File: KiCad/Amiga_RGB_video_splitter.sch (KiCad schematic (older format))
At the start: 14 parts, among them J1 DB23_Female-Connector, J2 DB15_Female_HighDensity_Mount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, J3 KMDGX-9S-BS-1, J4 PJ-320A, J5 Conn_01x03, U1 THS7374IPWR, U2 74HCT2G17

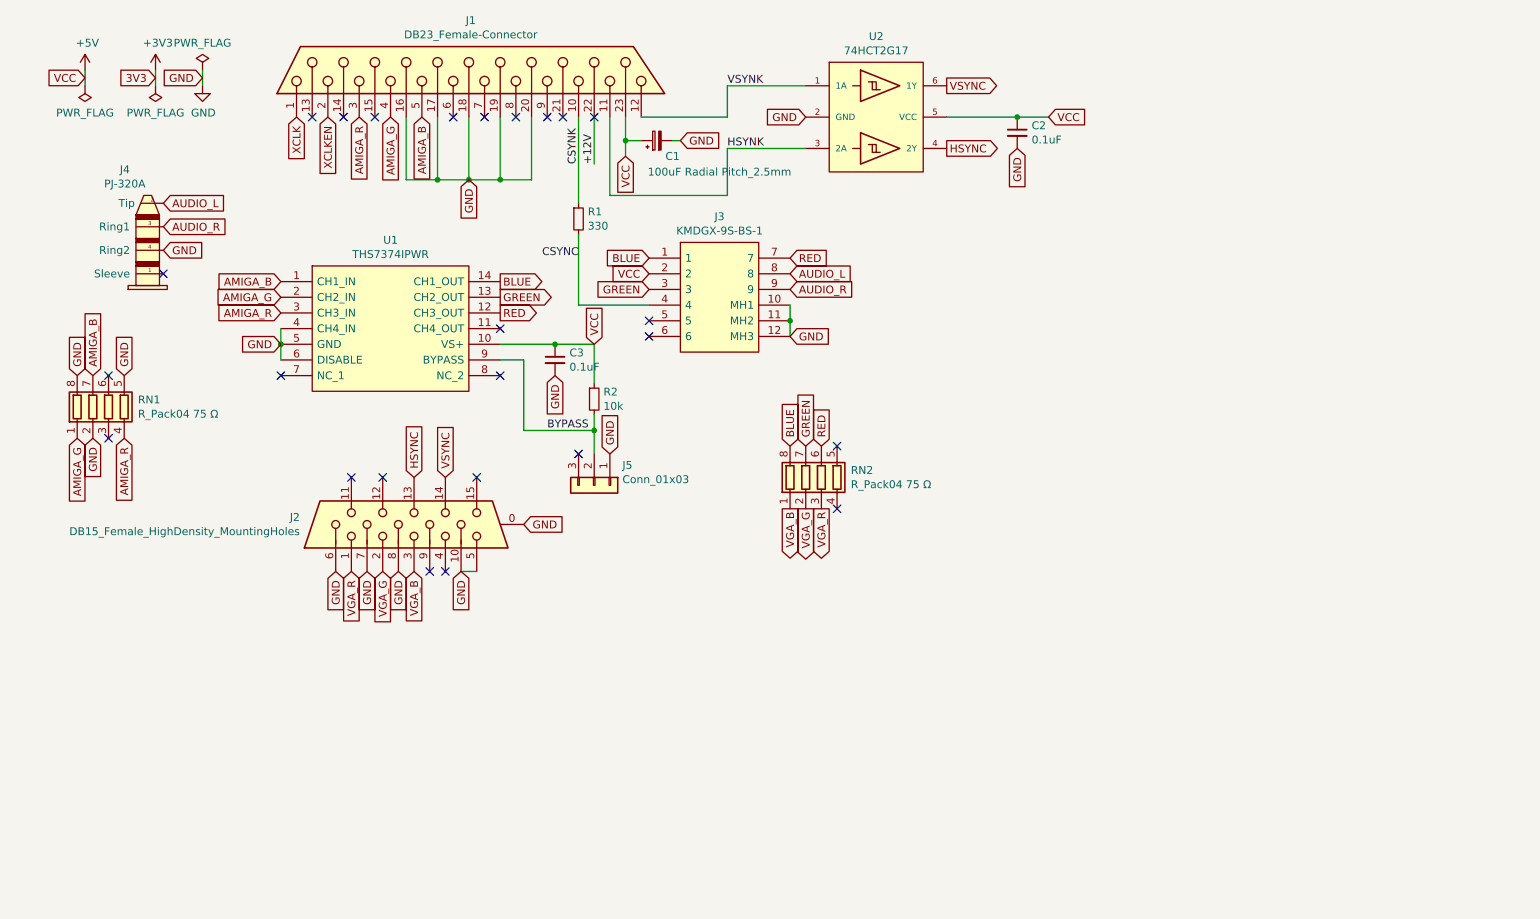
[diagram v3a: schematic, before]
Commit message: Add U3 (74HCT2G14) and R3,R4,C4,C5 to the design
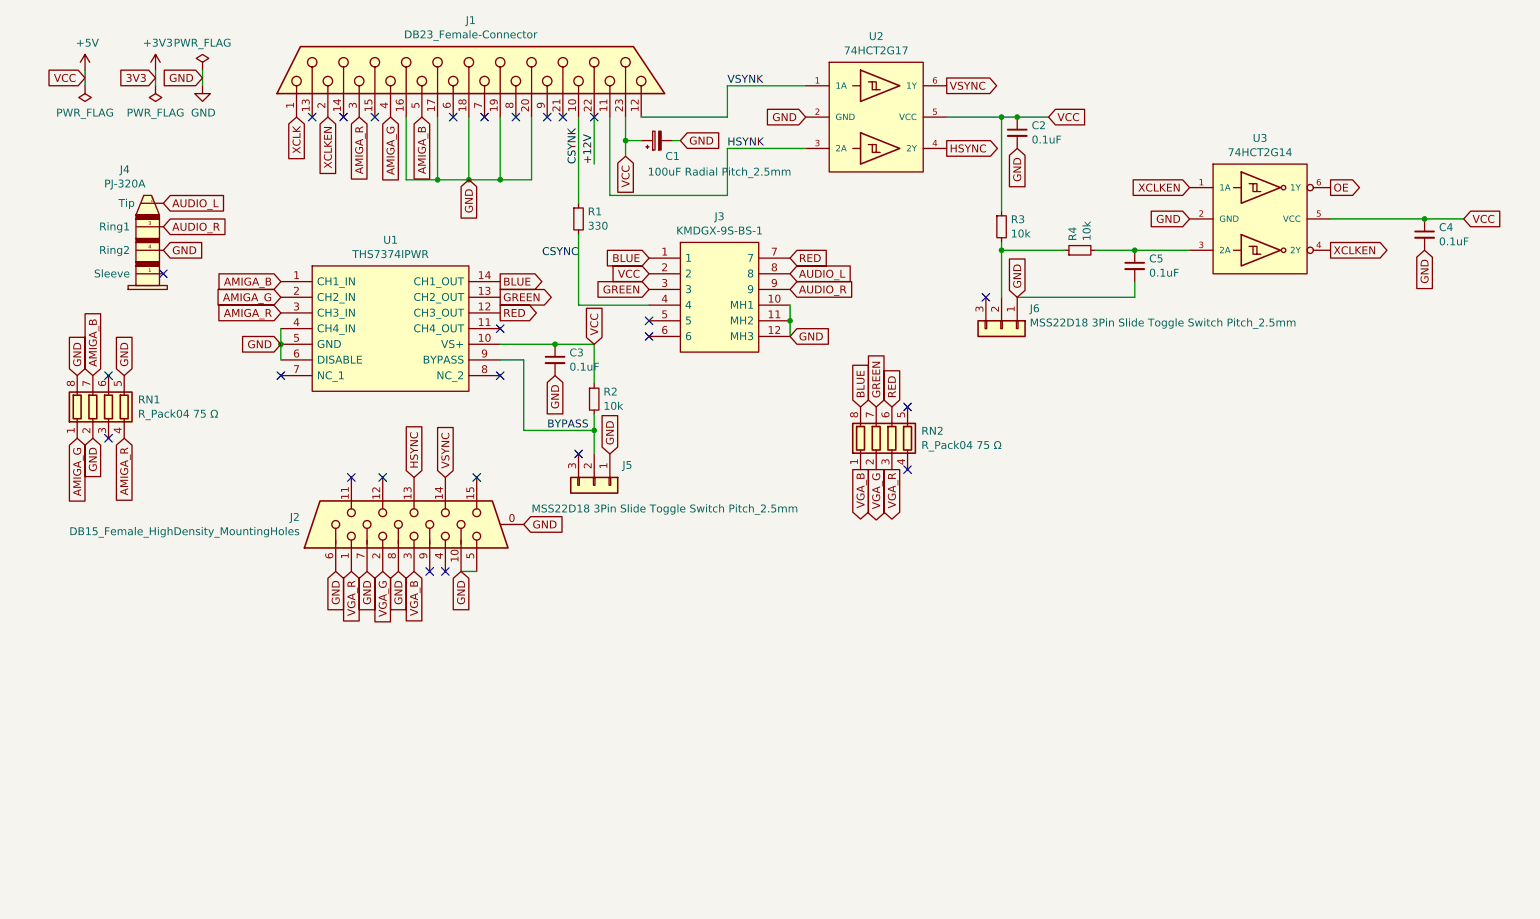
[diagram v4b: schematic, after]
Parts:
- added C4, C5: 0.1uF, Capacitor_SMD:C_0805_2012Metric_Pad1.18x1.45mm_HandSolder, symbol Device:C_Small
- added J6: MSS22D18 3Pin Slide Toggle Switch Pitch_2.5mm, Amiga_RGB_video_splitter:PinHeader_1x03_P2.5mm_Vertical, symbol Connector_Generic:Conn_01x03
- added R3, R4: 10k, Resistor_SMD:R_1206_3216Metric_Pad1.30x1.75mm_HandSolder, symbol Device:R_Small
- added U3: 74HCT2G14, Package_SO:TSOP-6_1.65x3.05mm_P0.95mm, symbol Amiga_RGB_video_splitter:74HCT2G14
- J5: value Conn_01x03 -> MSS22D18 3Pin Slide Toggle Switch Pitch_2.5mm
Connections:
- net +5V: now also C4.1, R3.1, U3.5 (VCC)
- net GND: now also C4.2, C5.2, J6.1 (Pin_1), U3.2 (GND)
- net XCLKEN: now also U3.1 (1A), U3.4 (2Y)
- new net: J6.2 (Pin_2), R3.2, R4.1
- new net: C5.1, R4.2, U3.3 (2A)
- new net OE: U3.6 (1Y)
- no-connect marks 25 -> 26
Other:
- moved on the sheet: RN2
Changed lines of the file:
@@
 L Device:R_Pack04 RN2
 U 1 1 68354B66
-P 5850 5000
-F 0 "RN2" H 6038 5046 50  0000 L CNN
-F 1 "R_Pack04 75 Ω" H 6038 4955 50  0000 L CNN
-F 2 "Amiga_RGB_video_splitter:RESCAF80P320X160X60-8N" V 6125 5000 50  0001 C CNN
-F 3 "~" H 5850 5000 50  0001 C CNN
-	1    5850 5000
-	1    0    0    -1
-$EndComp
-Text GLabel 5650 4800 1    50   Input ~ 0
+P 6300 4750
+F 0 "RN2" H 6488 4796 50  0000 L CNN
+F 1 "R_Pack04 75 Ω" H 6488 4705 50  0000 L CNN
+F 2 "Amiga_RGB_video_splitter:RESCAF80P320X160X60-8N" V 6575 4750 50  0001 C CNN
+F 3 "~" H 6300 4750 50  0001 C CNN
+	1    6300 4750
+	1    0    0    -1
+$EndComp
+Text GLabel 6100 4550 1    50   Input ~ 0
 BLUE
-Text GLabel 5750 4800 1    50   Input ~ 0
+Text GLabel 6200 4550 1    50   Input ~ 0
 GREEN
-Text GLabel 5850 4800 1    50   Input ~ 0
+Text GLabel 6300 4550 1    50   Input ~ 0
 RED
-Text GLabel 5650 5200 3    50   Output ~ 0
+Text GLabel 6100 4950 3    50   Output ~ 0
 VGA_B
-Text GLabel 5750 5200 3    50   Output ~ 0
+Text GLabel 6200 4950 3    50   Output ~ 0
 VGA_G
-Text GLabel 5850 5200 3    50   Output ~ 0
+Text GLabel 6300 4950 3    50   Output ~ 0
 VGA_R
 $Comp
@@
 VSYNK
 Wire Wire Line
-	6650 2700 7100 2700
+	6650 2700 7000 2700
 Wire Wire Line
 	5250 2900 5750 2900
 Text Label 5250 2900 0    50   ~ 0
 HSYNK
-NoConn ~ 5950 4800
-NoConn ~ 5950 5200
+NoConn ~ 6400 4550
+NoConn ~ 6400 4950
 $Comp
 L Device:CP_Small C1
@@
 P 4400 5050
 F 0 "J5" V 4272 5230 50  0000 L CNN
-F 1 "Conn_01x03" V 4363 5230 50  0000 L CNN
+F 1 "MSS22D18 3Pin Slide Toggle Switch Pitch_2.5mm" V 4550 4650 50  0000 L CNN
 F 2 "Amiga_RGB_video_splitter:PinHeader_1x03_P2.5mm_Vertical" H 4400 5050 50  0001 C CNN
 F 3 "~" H 4400 5050 50  0001 C CNN
@@
 	4400 4600 4400 4700
 Connection ~ 4400 4700
+$Comp
+L Connector_Generic:Conn_01x03 J6
+U 1 1 6837A004
+P 7000 4050
+F 0 "J6" V 6872 4230 50  0000 L CNN
+F 1 "MSS22D18 3Pin Slide Toggle Switch Pitch_2.5mm" V 6963 4230 50  0000 L CNN
+F 2 "Amiga_RGB_video_splitter:PinHeader_1x03_P2.5mm_Vertical" H 7000 4050 50  0001 C CNN
+F 3 "~" H 7000 4050 50  0001 C CNN
+	1    7000 4050
+	0    1    1    0
+$EndComp
+Text GLabel 7100 3850 1    50   Input ~ 0
+GND
+$Comp
+L Device:R_Small R3
+U 1 1 6837CDA8
+P 7000 3400
+F 0 "R3" H 7059 3446 50  0000 L CNN
+F 1 "10k" H 7059 3355 50  0000 L CNN
+F 2 "Resistor_SMD:R_1206_3216Metric_Pad1.30x1.75mm_HandSolder" H 7000 3400 50  0001 C CNN
+F 3 "~" H 7000 3400 50  0001 C CNN
+	1    7000 3400
+	1    0    0    -1
+$EndComp
+Wire Wire Line
+	7000 3300 7000 2700
+Connection ~ 7000 2700
+Wire Wire Line
+	7000 2700 7100 2700
+Wire Wire Line
+	7000 3500 7000 3550
+$Comp
+L Amiga_RGB_video_splitter:74HCT2G14 U3
+U 1 1 6838826B
+P 8650 3350
+F 0 "U3" H 8650 3865 50  0000 C CNN
+F 1 "74HCT2G14" H 8650 3774 50  0000 C CNN
+F 2 "Package_SO:TSOP-6_1.65x3.05mm_P0.95mm" H 9150 4300 50  0001 C CNN
+F 3 "https://assets.nexperia.com/documents/data-sheet/74HC_HCT2G14.pdf" H 9150 4300 50  0001 C CNN
+	1    8650 3350
+	1    0    0    -1
+$EndComp
+Text GLabel 8200 3350 0    50   Input ~ 0
+GND
+Text GLabel 9950 3350 2    50   Input ~ 0
+VCC
+NoConn ~ 6900 3850
+$Comp
+L Device:R_Small R4
+U 1 1 68395832
+P 7500 3550
+F 0 "R4" H 7559 3596 50  0000 L CNN
+F 1 "10k" H 7559 3505 50  0000 L CNN
+F 2 "Resistor_SMD:R_1206_3216Metric_Pad1.30x1.75mm_HandSolder" H 7500 3550 50  0001 C CNN
+F 3 "~" H 7500 3550 50  0001 C CNN
+	1    7500 3550
+	0    -1   -1   0
+$EndComp
+$Comp
+L Device:C_Small C4
+U 1 1 683963DB
+P 9700 3450
+F 0 "C4" H 9792 3496 50  0000 L CNN
+F 1 "0.1uF" H 9792 3405 50  0000 L CNN
+F 2 "Capacitor_SMD:C_0805_2012Metric_Pad1.18x1.45mm_HandSolder" H 9700 3450 50  0001 C CNN
+F 3 "~" H 9700 3450 50  0001 C CNN
+	1    9700 3450
+	1    0    0    -1
+$EndComp
+Text GLabel 9700 3550 3    50   Input ~ 0
+GND
+Wire Wire Line
+	9950 3350 9700 3350
+Connection ~ 9700 3350
+$Comp
+L Device:C_Small C5
+U 1 1 6839C207
+P 7850 3650
+F 0 "C5" H 7942 3696 50  0000 L CNN
+F 1 "0.1uF" H 7942 3605 50  0000 L CNN
+F 2 "Capacitor_SMD:C_0805_2012Metric_Pad1.18x1.45mm_HandSolder" H 7850 3650 50  0001 C CNN
+F 3 "~" H 7850 3650 50  0001 C CNN
+	1    7850 3650
+	1    0    0    -1
+$EndComp
+Wire Wire Line
+	7400 3550 7000 3550
+Connection ~ 7000 3550
+Wire Wire Line
+	7000 3550 7000 3850
+Wire Wire Line
+	7600 3550 7850 3550
+Connection ~ 7850 3550
+Wire Wire Line
+	7850 3550 8200 3550
+Wire Wire Line
+	7100 3850 7850 3850
+Wire Wire Line
+	7850 3850 7850 3750
+Text GLabel 9100 3550 2    50   Output ~ 0
+XCLKEN
+Wire Wire Line
+	9100 3350 9700 3350
+Text GLabel 8200 3150 0    50   Input ~ 0
+XCLKEN
+Text GLabel 9100 3150 2    50   Output ~ 0
+OE
 $EndSCHEMATC

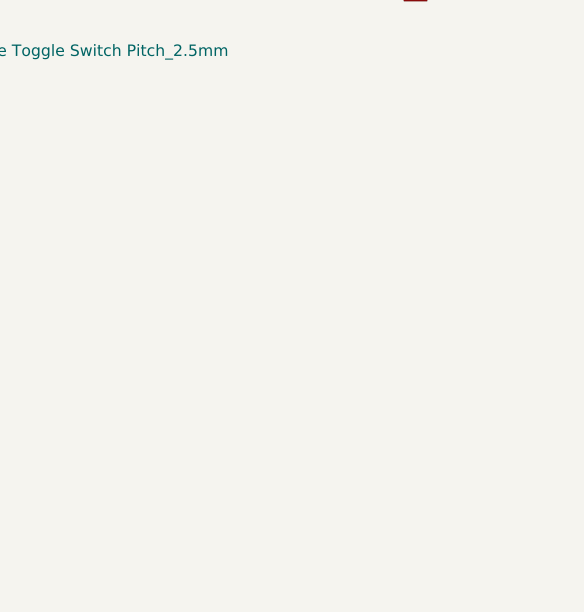
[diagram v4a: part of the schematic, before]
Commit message: Add U4 (74LVC1GX04) to the design
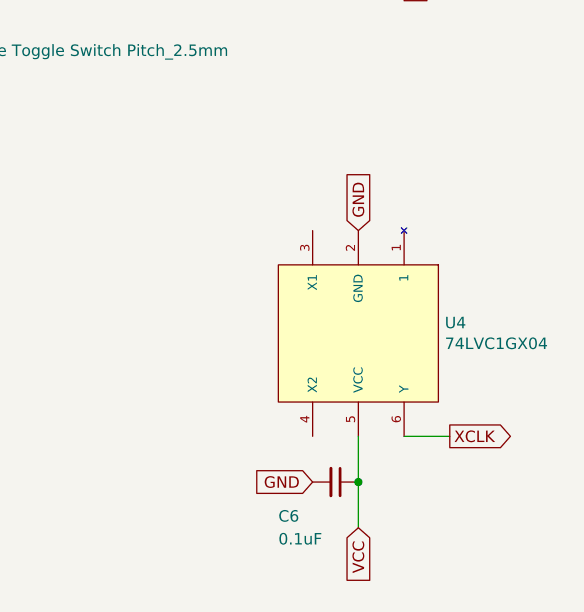
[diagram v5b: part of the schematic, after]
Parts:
- added C6: 0.1uF, Capacitor_SMD:C_0805_2012Metric_Pad1.18x1.45mm_HandSolder, symbol Device:C_Small
- added U4: 74LVC1GX04, Package_SO:TSOP-6_1.65x3.05mm_P0.95mm, symbol Amiga_RGB_video_splitter:74LVC1GX04
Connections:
- net +5V: now also C6.1, U4.5 (VCC)
- net GND: now also C6.2, U4.2 (GND)
- net XCLK: now also U4.6 (Y)
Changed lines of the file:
@@
 Text GLabel 9100 3150 2    50   Output ~ 0
 OE
+$Comp
+L Amiga_RGB_video_splitter:74LVC1GX04 U4
+U 1 1 683CA8F1
+P 9450 5250
+F 0 "U4" V 9404 5628 50  0000 L CNN
+F 1 "74LVC1GX04" V 9495 5628 50  0000 L CNN
+F 2 "Package_SO:TSOP-6_1.65x3.05mm_P0.95mm" H 9950 6200 50  0001 C CNN
+F 3 "https://www.mouser.se/datasheet/2/916/74LVC1GX04-2937637.pdf" H 9950 6200 50  0001 C CNN
+	1    9450 5250
+	0    1    1    0
+$EndComp
+Text GLabel 9450 4800 1    50   Input ~ 0
+GND
+Text GLabel 9450 6100 3    50   Input ~ 0
+VCC
+$Comp
+L Device:C_Small C6
+U 1 1 683CD4B5
+P 9350 5900
+F 0 "C6" V 9500 5650 50  0000 L CNN
+F 1 "0.1uF" V 9600 5650 50  0000 L CNN
+F 2 "Capacitor_SMD:C_0805_2012Metric_Pad1.18x1.45mm_HandSolder" H 9350 5900 50  0001 C CNN
+F 3 "~" H 9350 5900 50  0001 C CNN
+	1    9350 5900
+	0    1    1    0
+$EndComp
+Text GLabel 9250 5900 0    50   Input ~ 0
+GND
+Wire Wire Line
+	9450 5700 9450 5900
+Connection ~ 9450 5900
+Wire Wire Line
+	9450 5900 9450 6100
+Text GLabel 9850 5700 2    50   Output ~ 0
+XCLK
+Wire Wire Line
+	9650 5700 9850 5700
 $EndSCHEMATC

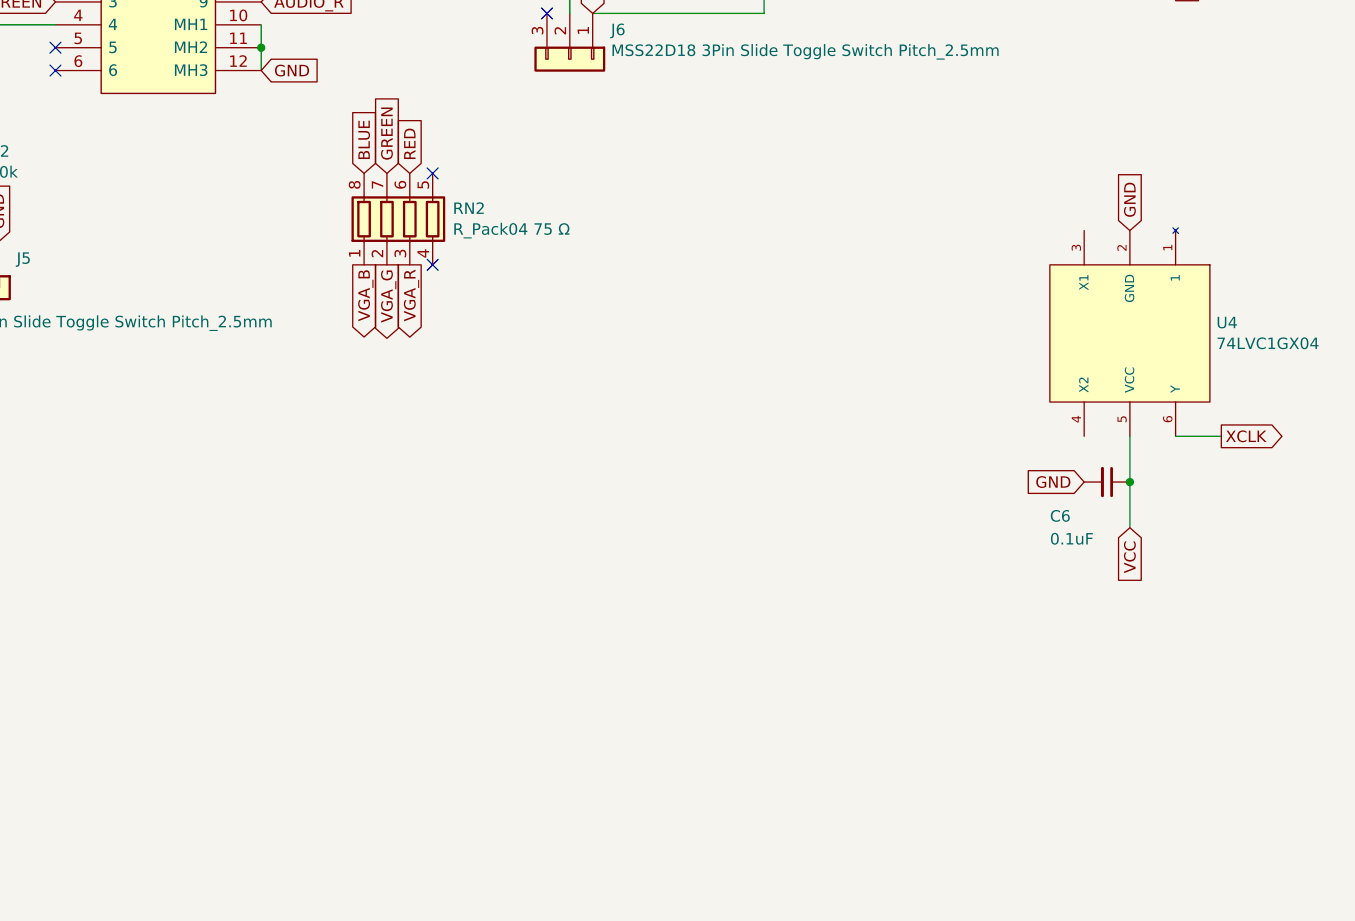
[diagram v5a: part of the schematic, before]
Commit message: Placement and routing of U4 (74LVC1GX04)
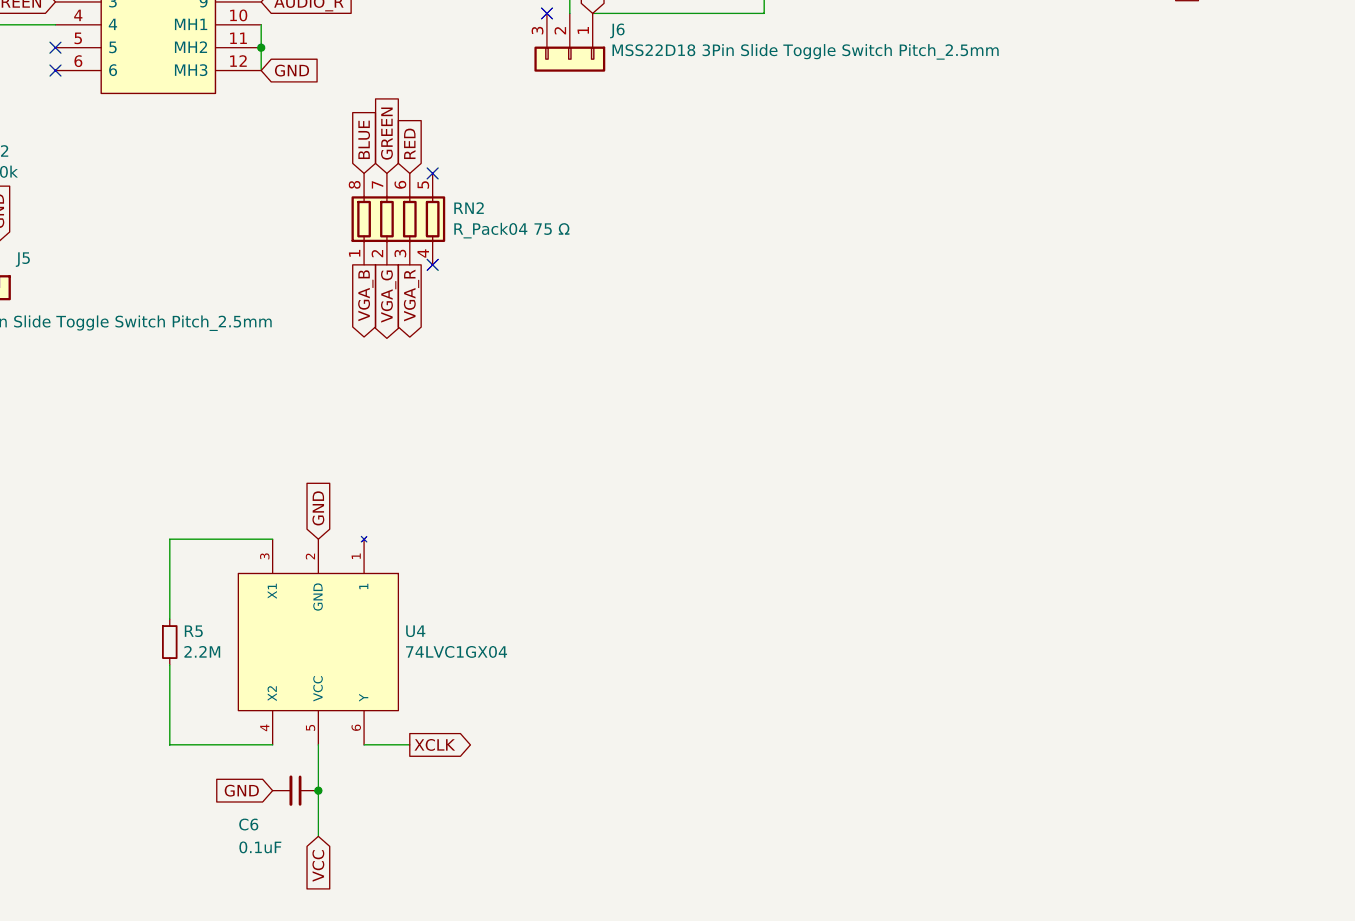
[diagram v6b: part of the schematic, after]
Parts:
- added R5: 2.2M, Resistor_SMD:R_0603_1608Metric_Pad0.98x0.95mm_HandSolder, symbol Device:R_Small
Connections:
- net at U4.3 (X1): now also R5.1
- net at U4.4 (X2): now also R5.2
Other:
- moved on the sheet: C6, U4
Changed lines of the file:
@@
 L Amiga_RGB_video_splitter:74LVC1GX04 U4
 U 1 1 683CA8F1
-P 9450 5250
-F 0 "U4" V 9404 5628 50  0000 L CNN
-F 1 "74LVC1GX04" V 9495 5628 50  0000 L CNN
-F 2 "Package_SO:TSOP-6_1.65x3.05mm_P0.95mm" H 9950 6200 50  0001 C CNN
-F 3 "https://www.mouser.se/datasheet/2/916/74LVC1GX04-2937637.pdf" H 9950 6200 50  0001 C CNN
-	1    9450 5250
+P 5900 6600
+F 0 "U4" V 5854 6978 50  0000 L CNN
+F 1 "74LVC1GX04" V 5945 6978 50  0000 L CNN
+F 2 "Package_SO:TSOP-6_1.65x3.05mm_P0.95mm" H 6400 7550 50  0001 C CNN
+F 3 "https://www.mouser.se/datasheet/2/916/74LVC1GX04-2937637.pdf" H 6400 7550 50  0001 C CNN
+	1    5900 6600
 	0    1    1    0
 $EndComp
-Text GLabel 9450 4800 1    50   Input ~ 0
+Text GLabel 5900 6150 1    50   Input ~ 0
 GND
-Text GLabel 9450 6100 3    50   Input ~ 0
+Text GLabel 5900 7450 3    50   Input ~ 0
 VCC
 $Comp
 L Device:C_Small C6
 U 1 1 683CD4B5
-P 9350 5900
-F 0 "C6" V 9500 5650 50  0000 L CNN
-F 1 "0.1uF" V 9600 5650 50  0000 L CNN
-F 2 "Capacitor_SMD:C_0805_2012Metric_Pad1.18x1.45mm_HandSolder" H 9350 5900 50  0001 C CNN
-F 3 "~" H 9350 5900 50  0001 C CNN
-	1    9350 5900
+P 5800 7250
+F 0 "C6" V 5950 7000 50  0000 L CNN
+F 1 "0.1uF" V 6050 7000 50  0000 L CNN
+F 2 "Capacitor_SMD:C_0805_2012Metric_Pad1.18x1.45mm_HandSolder" H 5800 7250 50  0001 C CNN
+F 3 "~" H 5800 7250 50  0001 C CNN
+	1    5800 7250
 	0    1    1    0
 $EndComp
-Text GLabel 9250 5900 0    50   Input ~ 0
+Text GLabel 5700 7250 0    50   Input ~ 0
 GND
 Wire Wire Line
-	9450 5700 9450 5900
-Connection ~ 9450 5900
+	5900 7050 5900 7250
+Connection ~ 5900 7250
 Wire Wire Line
-	9450 5900 9450 6100
-Text GLabel 9850 5700 2    50   Output ~ 0
+	5900 7250 5900 7450
+Text GLabel 6300 7050 2    50   Output ~ 0
 XCLK
 Wire Wire Line
-	9650 5700 9850 5700
+	6100 7050 6300 7050
+$Comp
+L Device:R_Small R5
+U 1 1 683E0C95
+P 5250 6600
+F 0 "R5" H 5309 6646 50  0000 L CNN
+F 1 "2.2M" H 5309 6555 50  0000 L CNN
+F 2 "Resistor_SMD:R_0603_1608Metric_Pad0.98x0.95mm_HandSolder" H 5250 6600 50  0001 C CNN
+F 3 "~" H 5250 6600 50  0001 C CNN
+	1    5250 6600
+	1    0    0    -1
+$EndComp
+Wire Wire Line
+	5250 6500 5250 6150
+Wire Wire Line
+	5250 6150 5700 6150
+Wire Wire Line
+	5700 7050 5250 7050
+Wire Wire Line
+	5250 7050 5250 6700
 $EndSCHEMATC
